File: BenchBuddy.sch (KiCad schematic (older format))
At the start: 0 parts

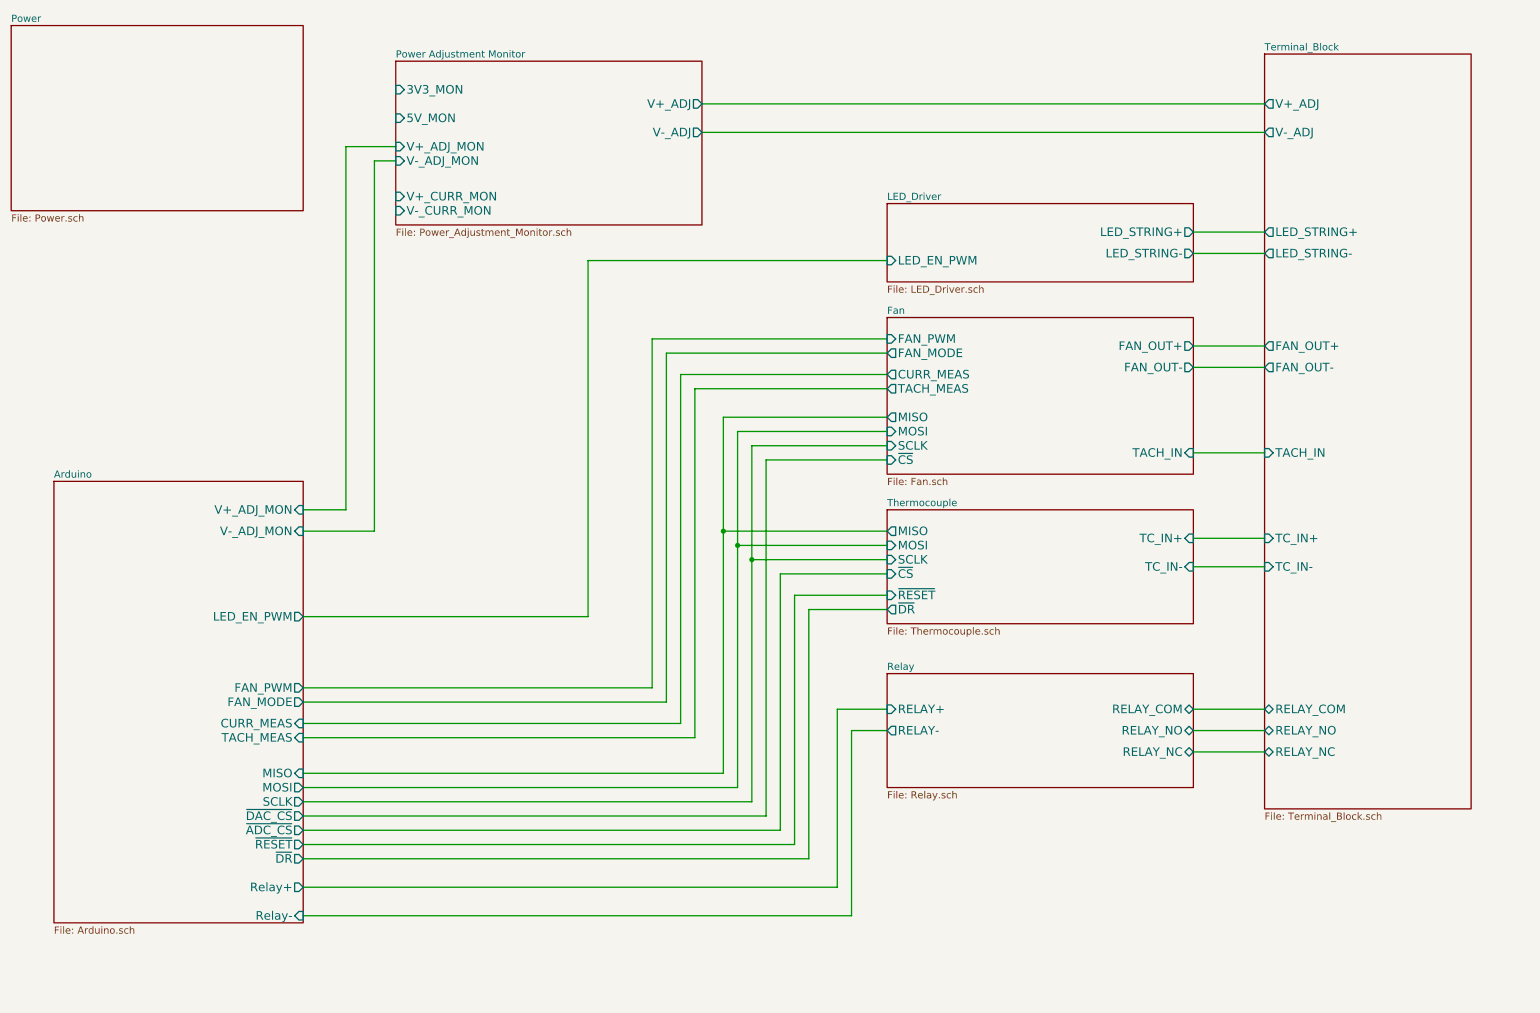
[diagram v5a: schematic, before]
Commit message: Associating and Placing the Current/Fan Driver Module
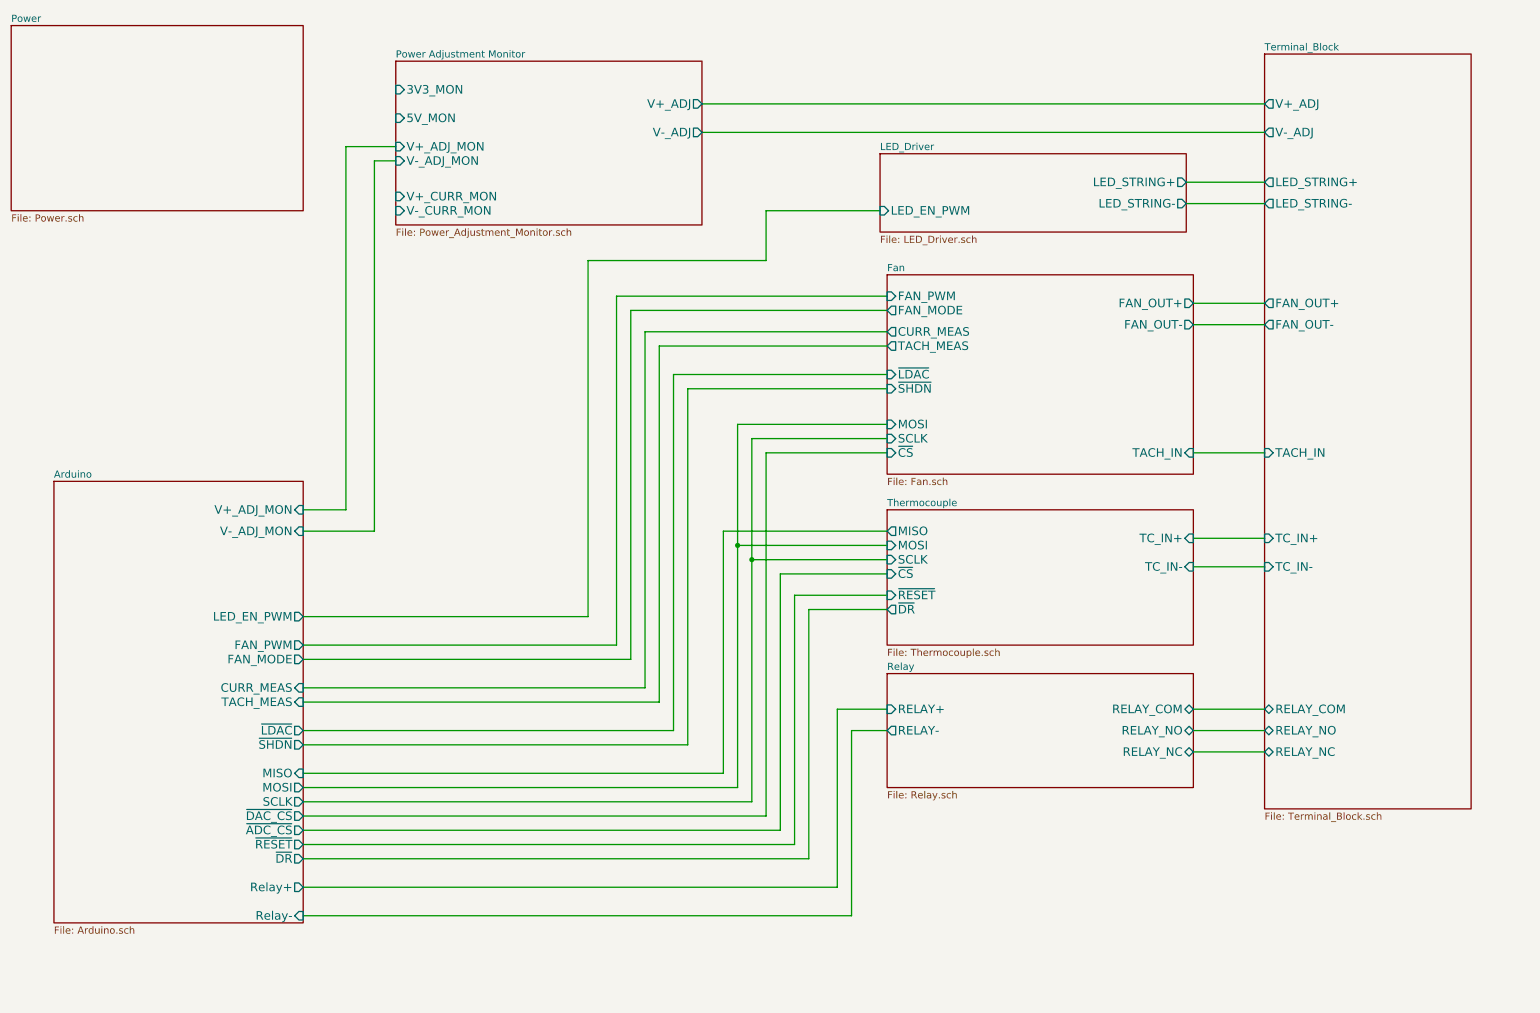
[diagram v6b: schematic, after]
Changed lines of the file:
@@
 F5 "MISO" I R 2650 5850 60
 F6 "SCLK" O R 2650 6050 60
-F7 "CURR_MEAS" I R 2650 5500 60
+F7 "CURR_MEAS" I R 2650 5250 60
 F8 "LED_EN_PWM" O R 2650 4750 60
-F9 "TACH_MEAS" I R 2650 5600 60
+F9 "TACH_MEAS" I R 2650 5350 60
 F10 "V+_ADJ_MON" I R 2650 4000 60
 F11 "V-_ADJ_MON" I R 2650 4150 60
-F12 "FAN_PWM" O R 2650 5250 60
-F13 "FAN_MODE" O R 2650 5350 60
+F12 "FAN_PWM" O R 2650 4950 60
+F13 "FAN_MODE" O R 2650 5050 60
 F14 "~DAC_CS" O R 2650 6150 60
 F15 "~ADC_CS" O R 2650 6250 60
 F16 "~RESET" O R 2650 6350 60
 F17 "~DR" O R 2650 6450 60
-$EndSheet
-$Sheet
-S 6750 4000 2150 800
+F18 "~LDAC" O R 2650 5550 60
+F19 "~SHDN" O R 2650 5650 60
+$EndSheet
+$Sheet
+S 6750 4000 2150 950
 U 52EA3553
 F0 "Thermocouple" 50
@@
 F2 "V+_ADJ" O L 9400 1150 60
 F3 "V-_ADJ" O L 9400 1350 60
-F4 "FAN_OUT+" O L 9400 2850 60
-F5 "FAN_OUT-" O L 9400 3000 60
+F4 "FAN_OUT+" O L 9400 2550 60
+F5 "FAN_OUT-" O L 9400 2700 60
 F6 "TACH_IN" I L 9400 3600 60
-F7 "LED_STRING+" O L 9400 2050 60
-F8 "LED_STRING-" O L 9400 2200 60
+F7 "LED_STRING+" O L 9400 1700 60
+F8 "LED_STRING-" O L 9400 1850 60
 F9 "RELAY_NC" B L 9400 5700 60
 F10 "RELAY_NO" B L 9400 5550 60
@@
 $EndSheet
 $Sheet
-S 6750 1850 2150 550
+S 6700 1500 2150 550
 U 52EA35F8
 F0 "LED_Driver" 50
 F1 "LED_Driver.sch" 50
-F2 "LED_EN_PWM" I L 6750 2250 60
-F3 "LED_STRING+" O R 8900 2050 60
-F4 "LED_STRING-" O R 8900 2200 60
+F2 "LED_EN_PWM" I L 6700 1900 60
+F3 "LED_STRING+" O R 8850 1700 60
+F4 "LED_STRING-" O R 8850 1850 60
 $EndSheet
 Wire Wire Line
@@
 	3150 1550 3300 1550
 $Sheet
-S 6750 2650 2150 1100
+S 6750 2350 2150 1400
 U 52EA3640
 F0 "Fan" 50
 F1 "Fan.sch" 50
-F2 "MISO" O L 6750 3350 60
-F3 "MOSI" I L 6750 3450 60
-F4 "SCLK" I L 6750 3550 60
-F5 "FAN_OUT+" O R 8900 2850 60
+F3 "MOSI" I L 6750 3400 60
+F4 "SCLK" I L 6750 3500 60
+F5 "FAN_OUT+" O R 8900 2550 60
 F6 "TACH_IN" I R 8900 3600 60
-F7 "TACH_MEAS" O L 6750 3150 60
-F8 "CURR_MEAS" O L 6750 3050 60
-F9 "FAN_OUT-" O R 8900 3000 60
-F10 "FAN_PWM" I L 6750 2800 60
-F11 "FAN_MODE" O L 6750 2900 60
-F12 "~CS" I L 6750 3650 60
-$EndSheet
-Wire Wire Line
-	9400 2050 8900 2050
-Wire Wire Line
-	8900 2200 9400 2200
-Wire Wire Line
-	9400 2850 8900 2850
-Wire Wire Line
-	8900 3000 9400 3000
+F7 "TACH_MEAS" O L 6750 2850 60
+F8 "CURR_MEAS" O L 6750 2750 60
+F9 "FAN_OUT-" O R 8900 2700 60
+F10 "FAN_PWM" I L 6750 2500 60
+F11 "FAN_MODE" O L 6750 2600 60
+F12 "~CS" I L 6750 3600 60
+F13 "~LDAC" I L 6750 3050 60
+F14 "~SHDN" I L 6750 3150 60
+$EndSheet
+Wire Wire Line
+	9400 2550 8900 2550
+Wire Wire Line
+	8900 2700 9400 2700
 Wire Wire Line
 	9400 3600 8900 3600
 Wire Wire Line
-	6750 2250 4650 2250
-Wire Wire Line
 	4650 2250 4650 4750
 Wire Wire Line
 	4650 4750 2650 4750
 Wire Wire Line
-	2650 5250 5100 5250
-Wire Wire Line
-	5100 5250 5100 2800
-Wire Wire Line
-	5100 2800 6750 2800
-Wire Wire Line
-	2650 5500 5300 5500
-Wire Wire Line
-	5300 5500 5300 3050
-Wire Wire Line
-	5300 3050 6750 3050
-Wire Wire Line
-	2650 5600 5400 5600
-Wire Wire Line
-	5400 5600 5400 3150
-Wire Wire Line
-	5400 3150 6750 3150
+	2650 4950 4850 4950
+Wire Wire Line
+	4850 4950 4850 2500
+Wire Wire Line
+	4850 2500 6750 2500
+Wire Wire Line
+	2650 5250 5050 5250
+Wire Wire Line
+	5050 5250 5050 2750
+Wire Wire Line
+	5050 2750 6750 2750
+Wire Wire Line
+	2650 5350 5150 5350
+Wire Wire Line
+	5150 5350 5150 2850
+Wire Wire Line
+	5150 2850 6750 2850
 Wire Wire Line
 	5600 5850 2650 5850
 Wire Wire Line
-	5600 3350 5600 5850
-Wire Wire Line
-	5600 3350 6750 3350
-Wire Wire Line
-	6750 3450 5700 3450
-Wire Wire Line
-	5700 3450 5700 5950
+	5600 4150 5600 5850
+Wire Wire Line
+	6750 3400 5700 3400
+Wire Wire Line
+	5700 3400 5700 5950
 Wire Wire Line
 	5700 5950 2650 5950
@@
 	5800 6050 2650 6050
 Wire Wire Line
-	5800 3550 5800 6050
-Wire Wire Line
-	5800 3550 6750 3550
+	5800 3500 5800 6050
+Wire Wire Line
+	5800 3500 6750 3500
 Wire Wire Line
 	6750 5400 6400 5400
@@
 	2650 6150 5900 6150
 Wire Wire Line
-	5900 6150 5900 3650
-Wire Wire Line
-	5900 3650 6750 3650
+	5900 6150 5900 3600
+Wire Wire Line
+	5900 3600 6750 3600
 Wire Wire Line
 	6750 4150 5600 4150
-Connection ~ 5600 4150
 Wire Wire Line
 	6750 4250 5700 4250
@@
 	6000 6250 2650 6250
 Wire Wire Line
-	6750 2900 5200 2900
-Wire Wire Line
-	5200 2900 5200 5350
-Wire Wire Line
-	5200 5350 2650 5350
+	6750 2600 4950 2600
+Wire Wire Line
+	4950 2600 4950 5050
+Wire Wire Line
+	4950 5050 2650 5050
 Wire Wire Line
 	2950 1450 2950 4000
@@
 Wire Wire Line
 	6200 6450 2650 6450
+Wire Wire Line
+	9400 1700 8850 1700
+Wire Wire Line
+	9400 1850 8850 1850
+Wire Wire Line
+	6700 1900 5900 1900
+Wire Wire Line
+	5900 1900 5900 2250
+Wire Wire Line
+	5900 2250 4650 2250
+Wire Wire Line
+	6750 3050 5250 3050
+Wire Wire Line
+	5250 3050 5250 5550
+Wire Wire Line
+	5250 5550 2650 5550
+Wire Wire Line
+	2650 5650 5350 5650
+Wire Wire Line
+	5350 5650 5350 3150
+Wire Wire Line
+	5350 3150 6750 3150
 $EndSCHEMATC
